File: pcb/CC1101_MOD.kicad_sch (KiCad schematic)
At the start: 23 parts, among them J11 Conn_Coaxial_Small, J12 Conn_01x07_Pin, U13 CC1101RGP, U14 ME6211C33M5, Y2 26Mhz

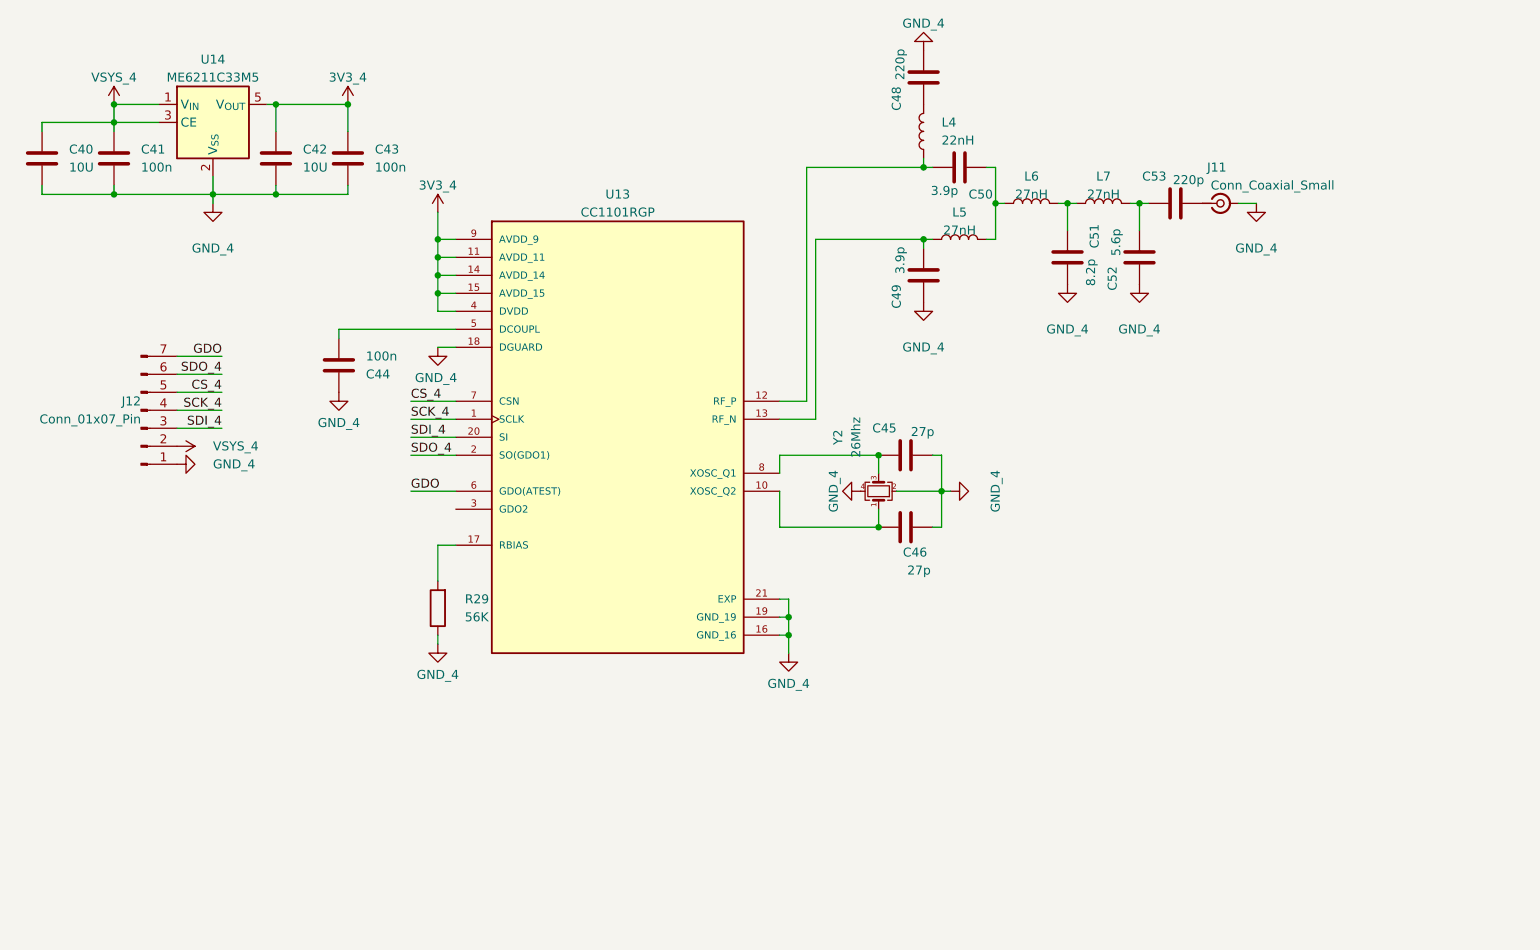
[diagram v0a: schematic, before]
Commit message: feat: improve pinout and remove sdcard and lora module, update design
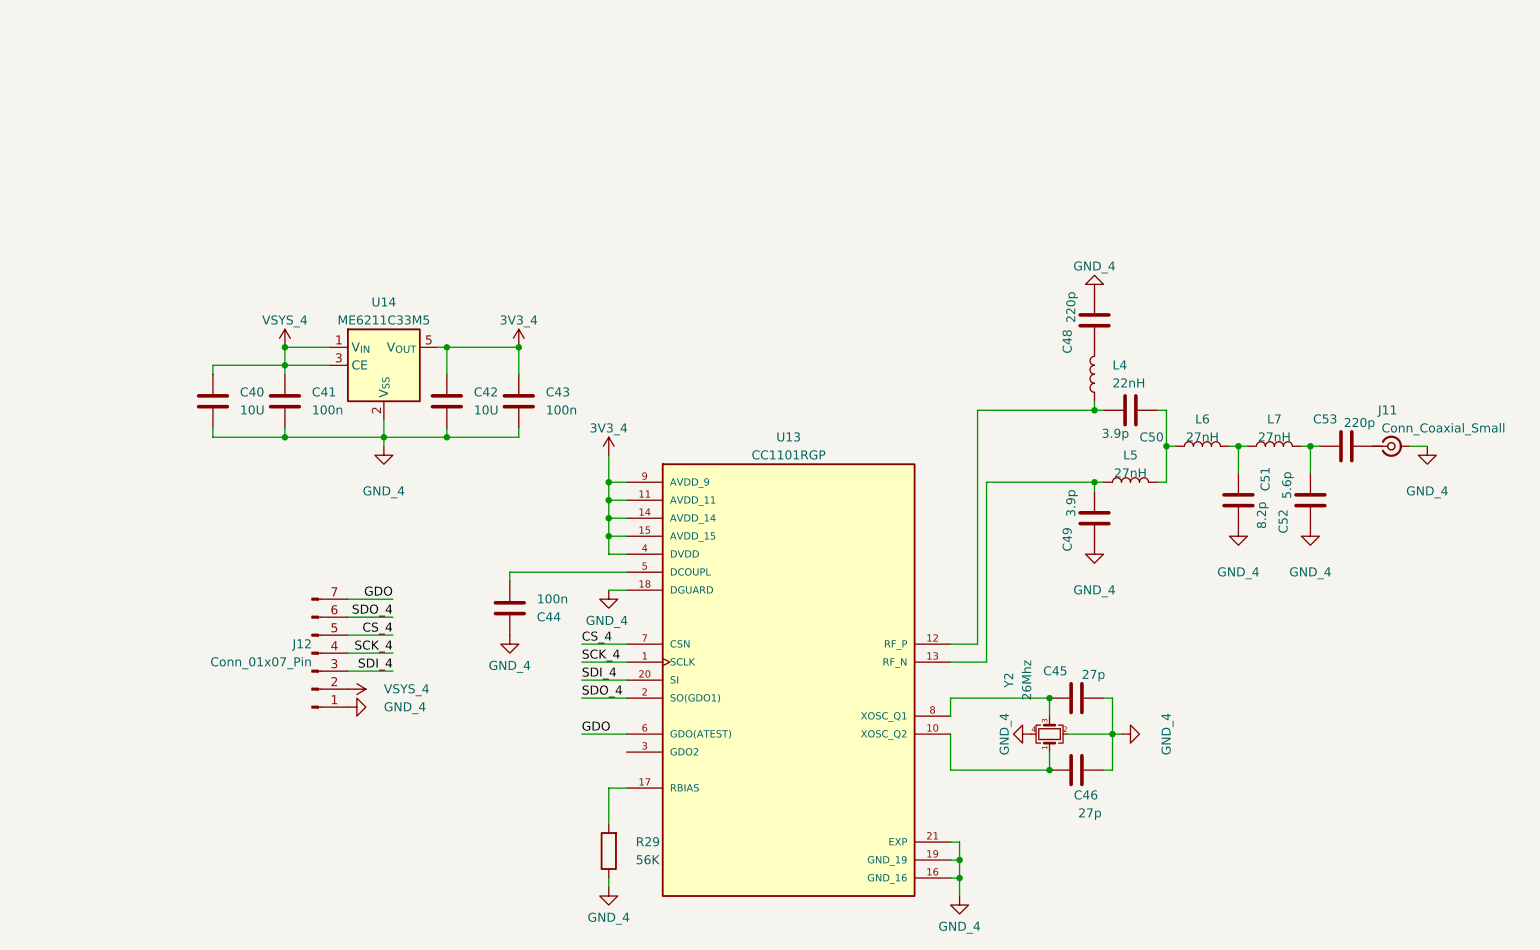
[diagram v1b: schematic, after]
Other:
- moved on the sheet: C40, C41, C42, C43, C44, C45, C46, C48, C49, C50, C51, C52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

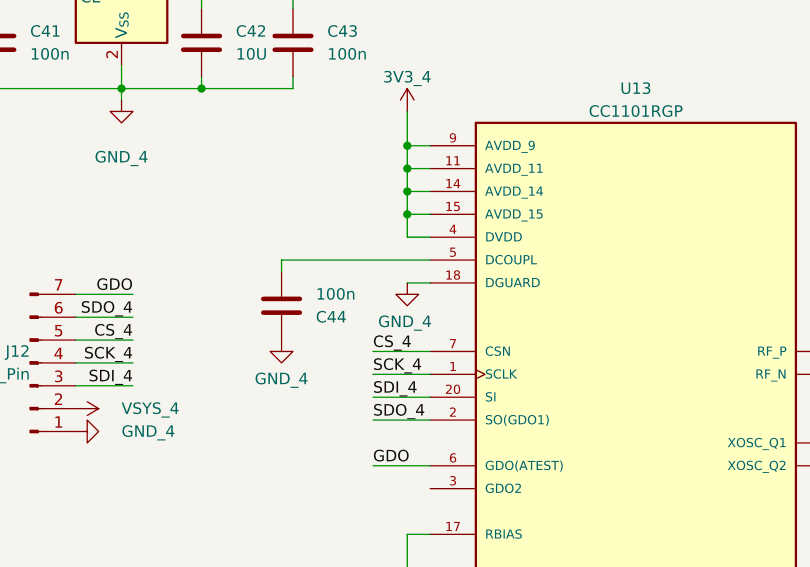
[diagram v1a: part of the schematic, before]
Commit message: fix sub ghz, epaper and audio module
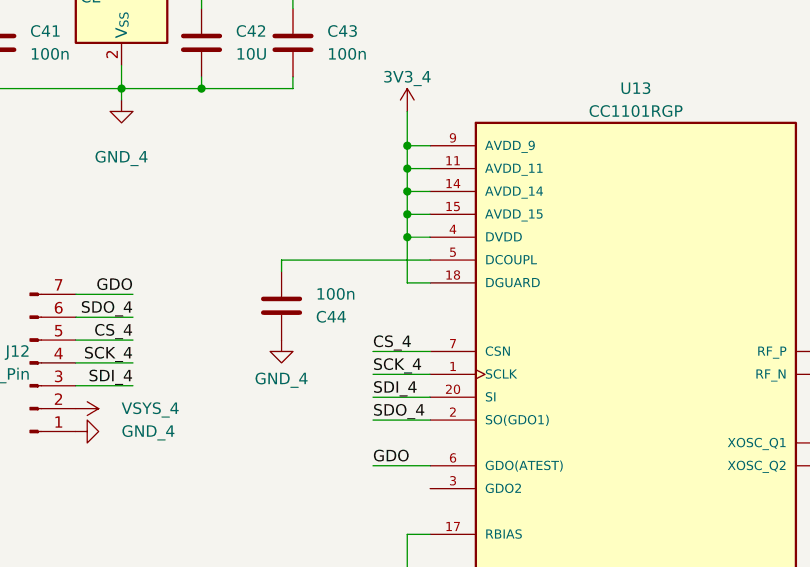
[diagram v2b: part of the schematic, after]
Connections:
- net 3V3_4: now also U13.18 (DGUARD)
- net GND_4: no longer U13.18 (DGUARD)
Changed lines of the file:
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@@
 		(color 0 0 0 0)
 	)
+	(junction
+		(at 113.03 93.98)
+		(diameter 0)
+		(color 0 0 0 0)
+	)
 	(wire
 		(pts
@@
 		(pts
 			(xy 109.22 111.76) (xy 115.57 111.76)
+		)
+		(stroke
+			(width 0)
+			(type default)
+		)
+	)
+	(wire
+		(pts
+			(xy 113.03 93.98) (xy 113.03 99.06)
 		)
 		(stroke
@@
 					(unit 1)
 				)
-			)
-		)
-	)
-	(symbol
-		(lib_id "power:GND")
-		(at 113.03 99.06 0)
-		(unit 1)
-		(exclude_from_sim no)
-		(in_bom yes)
-		(on_board yes)
-		(dnp no)
-		(property "Reference" "#PWR0125"
-			(at 113.03 105.41 0)
-			(effects
-				(font
-					(size 1.27 1.27)
-				)
-				(hide yes)
-			)
-		)
-		(property "Value" "GND_4"
-			(at 112.776 103.378 0)
-			(effects
-				(font
-					(size 1.27 1.27)
-				)
-			)
-		)
-		(property "Footprint" ""
-			(at 113.03 99.06 0)
-			(effects
-				(font
-					(size 1.27 1.27)
-				)
-				(hide yes)
-			)
-		)
-		(property "Datasheet" ""
-			(at 113.03 99.06 0)
-			(effects
-				(font
-					(size 1.27 1.27)
-				)
-				(hide yes)
-			)
-		)
-		(property "Description" "Power symbol creates a global label with name \"GND\" , ground"
-			(at 113.03 99.06 0)
-			(effects
-				(font
-					(size 1.27 1.27)
-				)
-				(hide yes)
-			)
-		)
-		(pin "1"
-		)
-		(instances
-			(project "lanyard"
-				(path "/96a9ebd7-4f87-4060-87a7-f00d27473ddc/1c85135a-c5d6-47ce-b7ac-c98d1b1d7c0d"
-					(reference "#PWR0125")
-					(unit 1)
-				)
